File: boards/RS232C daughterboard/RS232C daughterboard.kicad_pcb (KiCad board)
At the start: 2 copper layers, 14 parts, among them J202 DB9, P0 HEADER, U202 24AA014, U203 ISL83387E

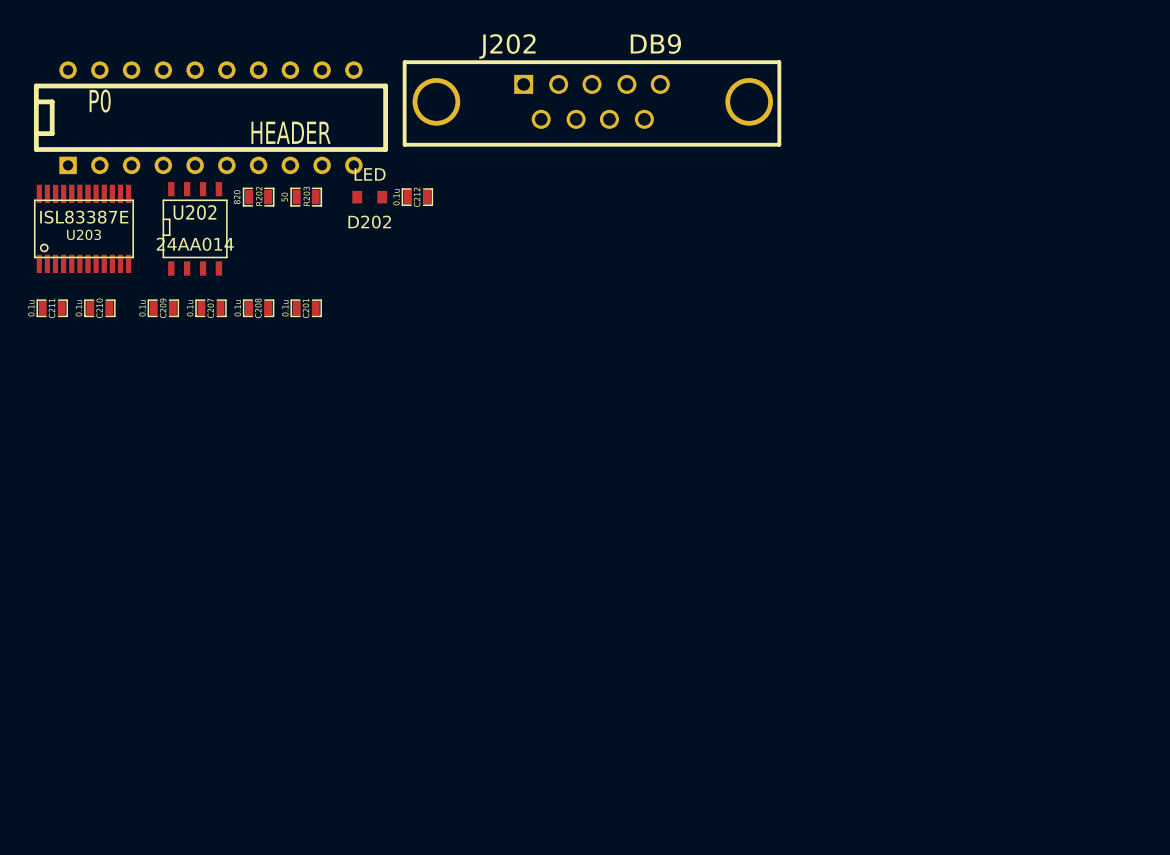
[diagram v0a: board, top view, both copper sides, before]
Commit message: Changed header to 10x2 pin array from DIP20 in RS232C dboard
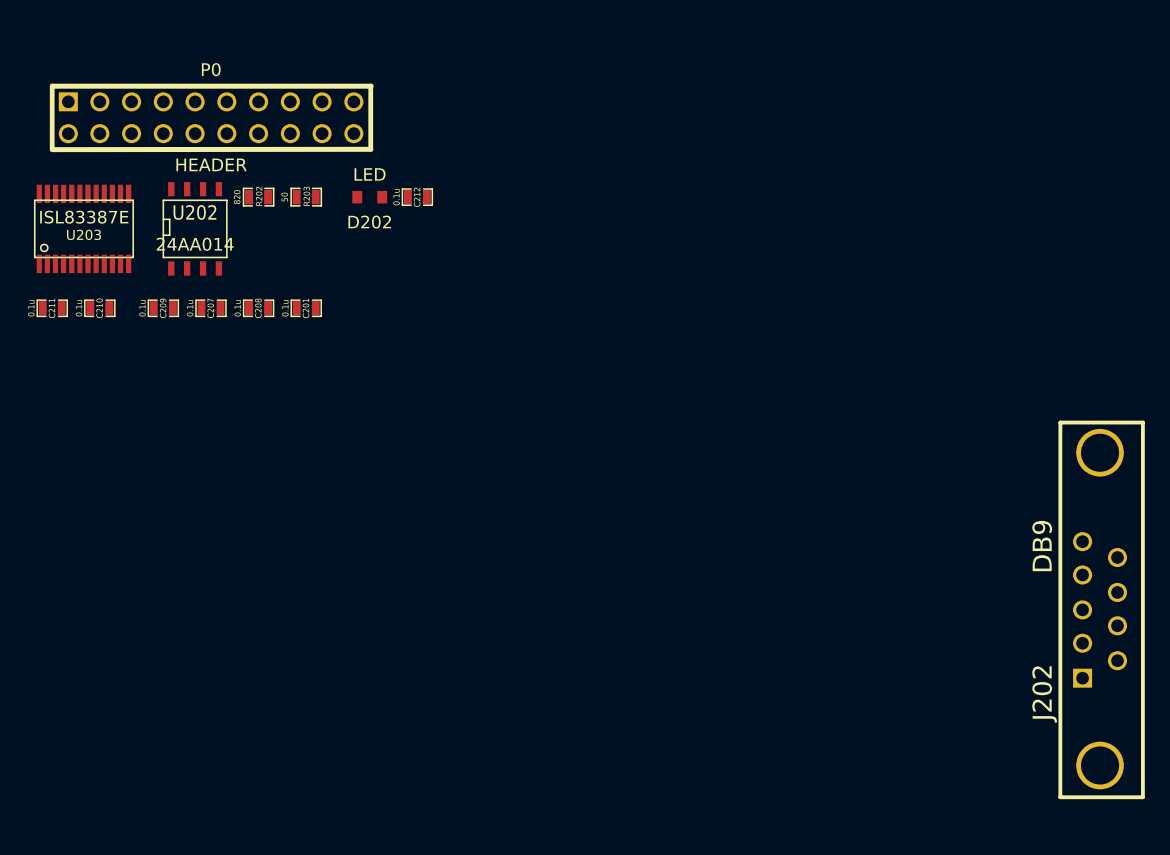
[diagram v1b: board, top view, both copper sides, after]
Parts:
- P0: footprint DIP-20__300 -> pin_array_10x2
- moved J202 57.5 mm to (90.2, 43.2), turned to 90 degrees

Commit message: Updated RS232C dboard to use new dboard_slot component
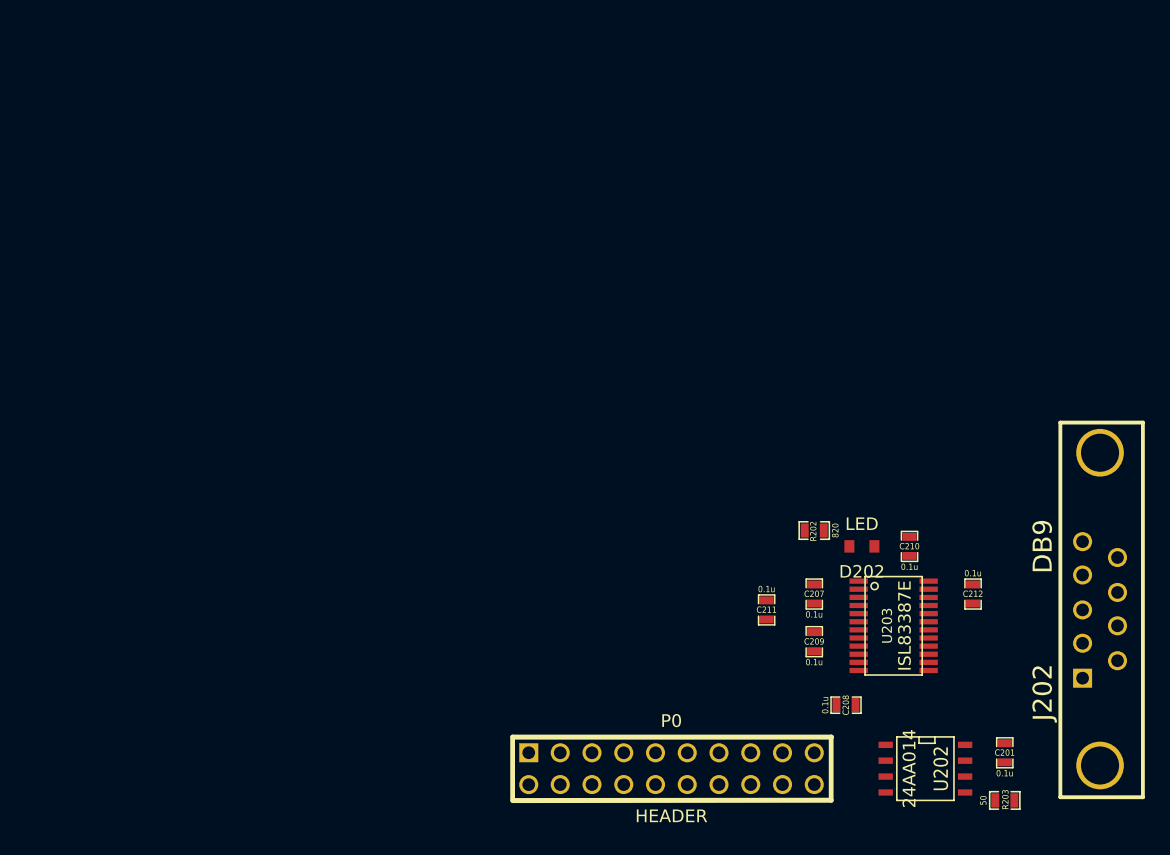
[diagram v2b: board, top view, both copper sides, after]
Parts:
- moved R203 73.8 mm to (82.5, 58.4)
- moved U202 72.6 mm to (76.2, 55.9), turned to 270 degrees
- moved U203 72.1 mm to (73.7, 44.5), turned to 270 degrees
- moved C210 67.5 mm to (74.9, 38.1), turned to 90 degrees
- moved C201 66.2 mm to (82.5, 54.6), turned to 90 degrees
- moved P0 63.8 mm to (55.9, 55.9)
- moved C211 62.0 mm to (63.5, 43.2), turned to 270 degrees
- moved C209 58.5 mm to (67.3, 45.7), turned to 90 degrees
- moved C208 56.7 mm to (69.8, 50.8)
- moved C212 54.6 mm to (80.0, 41.9), turned to 270 degrees
- moved C207 53.4 mm to (67.3, 41.9), turned to 90 degrees
- moved R202 51.8 mm to (67.3, 36.8), turned to 180 degrees
- moved D202 48.3 mm to (71.1, 38.1)
